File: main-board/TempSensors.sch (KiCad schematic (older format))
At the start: 0 parts

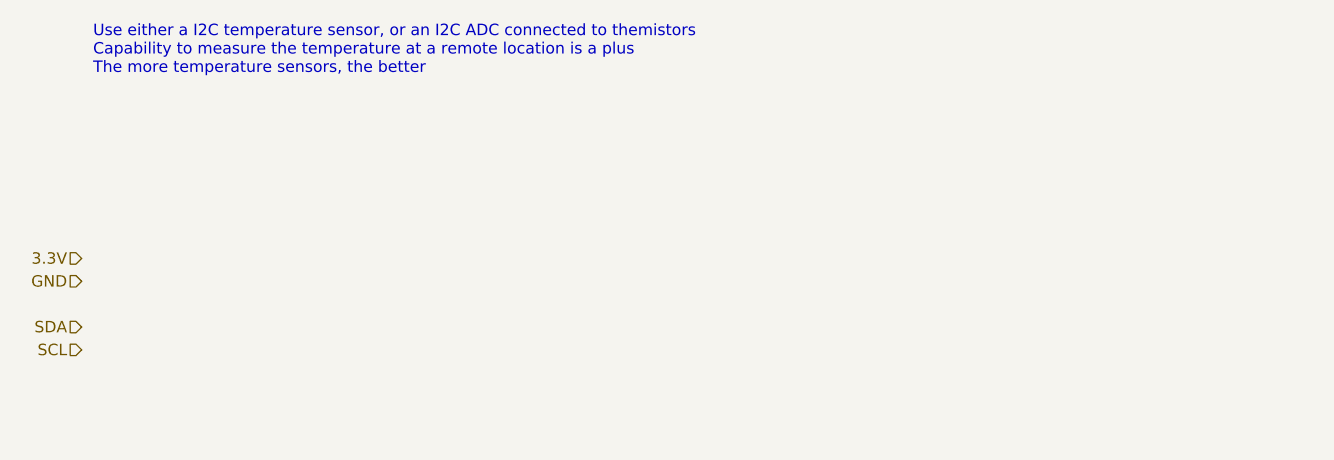
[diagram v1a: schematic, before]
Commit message: Even more subsheets
switched monitor and temp sensors to ADC. added temp sensors
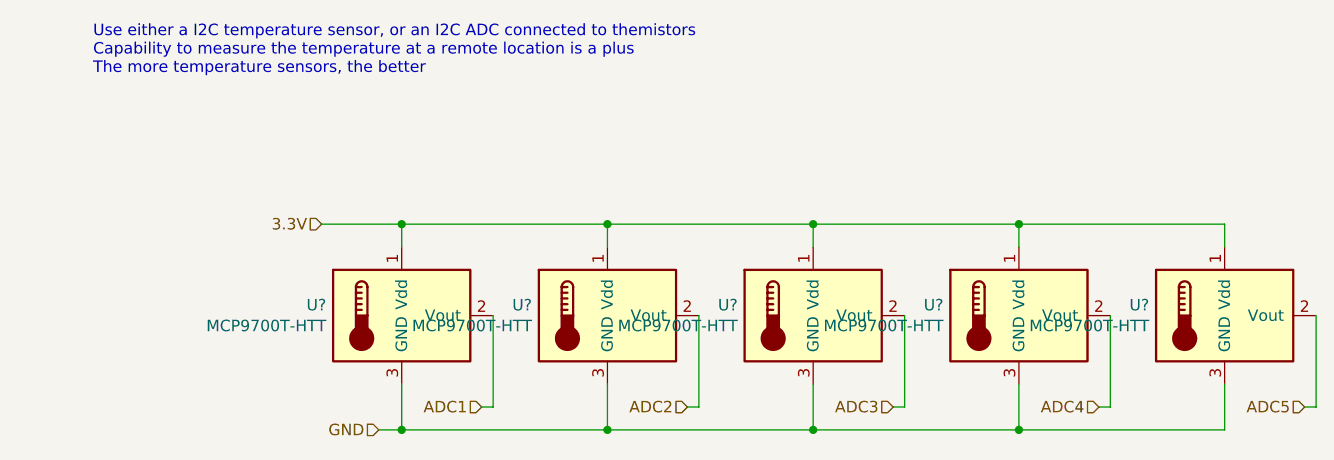
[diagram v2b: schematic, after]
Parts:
- added U? (x5): MCP9700T-HTT, Package_TO_SOT_SMD:SOT-23, symbol Sensor_Temperature:MCP9700T-HTT
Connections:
- net 3.3V: now also U?.1 (Vdd), U?.1 (Vdd), U?.1 (Vdd), U?.1 (Vdd), U?.1 (Vdd)
- net GND: now also U?.3 (GND), U?.3 (GND), U?.3 (GND), U?.3 (GND), U?.3 (GND)
- new net ADC1: U?.2 (Vout)
- new net ADC2: U?.2 (Vout)
- new net ADC3: U?.2 (Vout)
- new net ADC4: U?.2 (Vout)
- new net ADC5: U?.2 (Vout)
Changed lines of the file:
@@
 $Descr A4 11693 8268
 encoding utf-8
-Sheet 21 23
+Sheet 20 23
 Title ""
 Date ""
@@
 Comment4 ""
 $EndDescr
-Text HLabel 2500 3300 0    50   Input ~ 0
-SDA
-Text HLabel 2500 3400 0    50   Input ~ 0
-SCL
-Text HLabel 2500 3000 0    50   Input ~ 0
+Text HLabel 3550 2850 0    50   Input ~ 0
 3.3V
-Text HLabel 2500 3100 0    50   Input ~ 0
+Text HLabel 3800 3750 0    50   Input ~ 0
 GND
 Text Notes 2550 2200 0    50   ~ 0
 Use either a I2C temperature sensor, or an I2C ADC connected to themistors\nCapability to measure the temperature at a remote location is a plus\nThe more temperature sensors, the better
+Text HLabel 4250 3650 0    50   Input ~ 0
+ADC1
+$Comp
+L Sensor_Temperature:MCP9700T-HTT U?
+U 1 1 60C69F48
+P 3900 3250
+F 0 "U?" H 3570 3296 50  0000 R CNN
+F 1 "MCP9700T-HTT" H 3570 3205 50  0000 R CNN
+F 2 "Package_TO_SOT_SMD:SOT-23" H 3900 2850 50  0001 C CNN
+F 3 "http://ww1.microchip.com/downloads/en/DeviceDoc/21942e.pdf" H 3750 3500 50  0001 C CNN
+	1    3900 3250
+	1    0    0    -1
+$EndComp
+$Comp
+L Sensor_Temperature:MCP9700T-HTT U?
+U 1 1 60C6B7CB
+P 4800 3250
+F 0 "U?" H 4470 3296 50  0000 R CNN
+F 1 "MCP9700T-HTT" H 4470 3205 50  0000 R CNN
+F 2 "Package_TO_SOT_SMD:SOT-23" H 4800 2850 50  0001 C CNN
+F 3 "http://ww1.microchip.com/downloads/en/DeviceDoc/21942e.pdf" H 4650 3500 50  0001 C CNN
+	1    4800 3250
+	1    0    0    -1
+$EndComp
+$Comp
+L Sensor_Temperature:MCP9700T-HTT U?
+U 1 1 60C6CEC4
+P 5700 3250
+F 0 "U?" H 5370 3296 50  0000 R CNN
+F 1 "MCP9700T-HTT" H 5370 3205 50  0000 R CNN
+F 2 "Package_TO_SOT_SMD:SOT-23" H 5700 2850 50  0001 C CNN
+F 3 "http://ww1.microchip.com/downloads/en/DeviceDoc/21942e.pdf" H 5550 3500 50  0001 C CNN
+	1    5700 3250
+	1    0    0    -1
+$EndComp
+$Comp
+L Sensor_Temperature:MCP9700T-HTT U?
+U 1 1 60C6F08B
+P 6600 3250
+F 0 "U?" H 6270 3296 50  0000 R CNN
+F 1 "MCP9700T-HTT" H 6270 3205 50  0000 R CNN
+F 2 "Package_TO_SOT_SMD:SOT-23" H 6600 2850 50  0001 C CNN
+F 3 "http://ww1.microchip.com/downloads/en/DeviceDoc/21942e.pdf" H 6450 3500 50  0001 C CNN
+	1    6600 3250
+	1    0    0    -1
+$EndComp
+$Comp
+L Sensor_Temperature:MCP9700T-HTT U?
+U 1 1 60C6F091
+P 7500 3250
+F 0 "U?" H 7170 3296 50  0000 R CNN
+F 1 "MCP9700T-HTT" H 7170 3205 50  0000 R CNN
+F 2 "Package_TO_SOT_SMD:SOT-23" H 7500 2850 50  0001 C CNN
+F 3 "http://ww1.microchip.com/downloads/en/DeviceDoc/21942e.pdf" H 7350 3500 50  0001 C CNN
+	1    7500 3250
+	1    0    0    -1
+$EndComp
+Text HLabel 5150 3650 0    50   Input ~ 0
+ADC2
+Text HLabel 6050 3650 0    50   Input ~ 0
+ADC3
+Text HLabel 6950 3650 0    50   Input ~ 0
+ADC4
+Text HLabel 7850 3650 0    50   Input ~ 0
+ADC5
+Wire Wire Line
+	4300 3250 4300 3650
+Wire Wire Line
+	4300 3650 4250 3650
+Wire Wire Line
+	5200 3250 5200 3650
+Wire Wire Line
+	5200 3650 5150 3650
+Wire Wire Line
+	6100 3250 6100 3650
+Wire Wire Line
+	6100 3650 6050 3650
+Wire Wire Line
+	7000 3250 7000 3650
+Wire Wire Line
+	7000 3650 6950 3650
+Wire Wire Line
+	7900 3250 7900 3650
+Wire Wire Line
+	7900 3650 7850 3650
+Wire Wire Line
+	3550 2850 3900 2850
+Wire Wire Line
+	7500 2850 7500 2950
+Wire Wire Line
+	6600 2950 6600 2850
+Connection ~ 6600 2850
+Wire Wire Line
+	6600 2850 7500 2850
+Wire Wire Line
+	5700 2950 5700 2850
+Connection ~ 5700 2850
+Wire Wire Line
+	5700 2850 6600 2850
+Wire Wire Line
+	4800 2950 4800 2850
+Connection ~ 4800 2850
+Wire Wire Line
+	4800 2850 5700 2850
+Wire Wire Line
+	3900 2950 3900 2850
+Connection ~ 3900 2850
+Wire Wire Line
+	3900 2850 4800 2850
+Wire Wire Line
+	3800 3750 3900 3750
+Wire Wire Line
+	7500 3750 7500 3550
+Wire Wire Line
+	6600 3550 6600 3750
+Connection ~ 6600 3750
+Wire Wire Line
+	6600 3750 7500 3750
+Wire Wire Line
+	5700 3550 5700 3750
+Connection ~ 5700 3750
+Wire Wire Line
+	5700 3750 6600 3750
+Wire Wire Line
+	4800 3550 4800 3750
+Connection ~ 4800 3750
+Wire Wire Line
+	4800 3750 5700 3750
+Wire Wire Line
+	3900 3550 3900 3750
+Connection ~ 3900 3750
+Wire Wire Line
+	3900 3750 4800 3750
 $EndSCHEMATC
